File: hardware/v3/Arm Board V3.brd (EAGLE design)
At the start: 165.1 x 76.2 mm, 75 parts, among them CN1 1X4-BIG, IC1 L6206D, IC2 L6206D, IC3 L6206D, IC4 7812TV, IC5 7812TV, IC6 7812TV, IC7 7812DT, IC9 7812DT, Q3 Q_LTC490, U1 MAX3468CPA, U2 XBEE-1B3

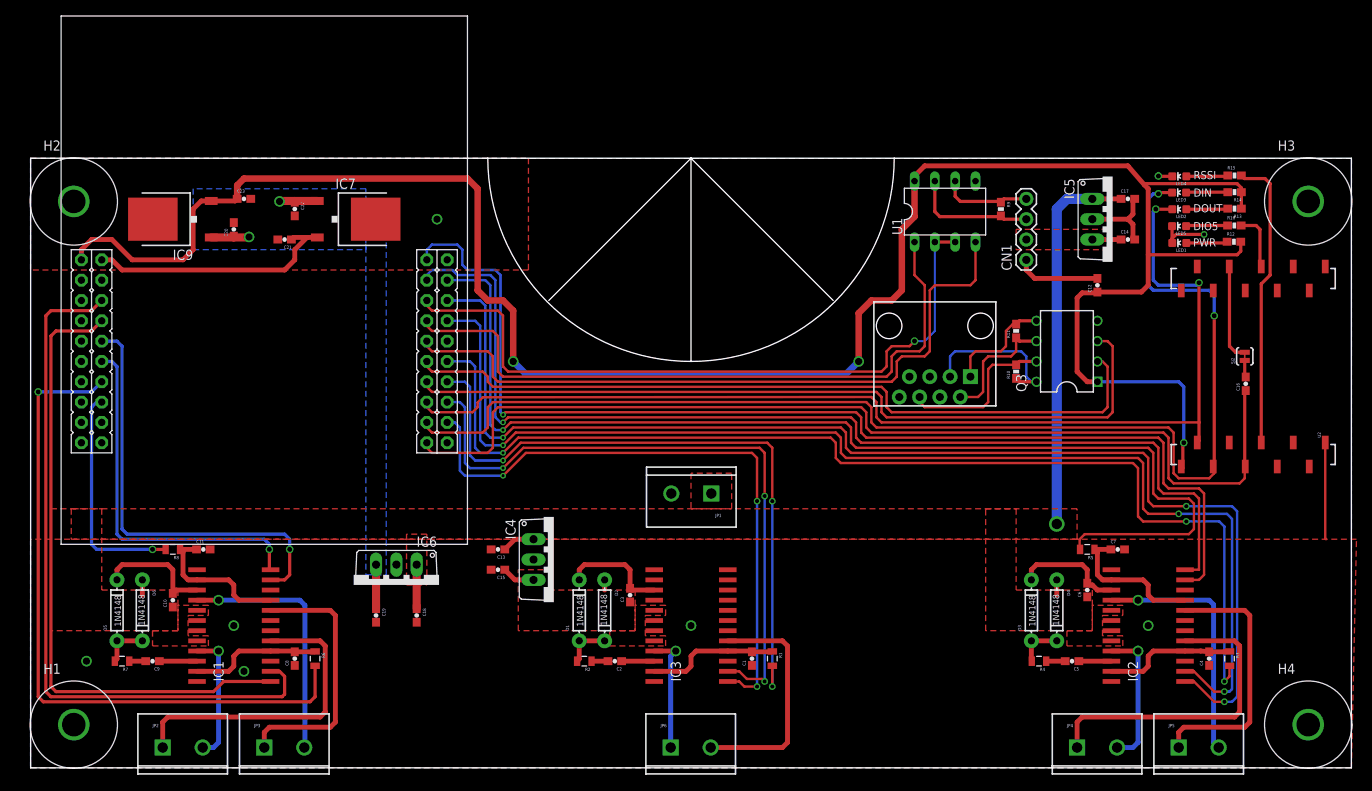
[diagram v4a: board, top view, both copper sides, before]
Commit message: Made some traces bigger
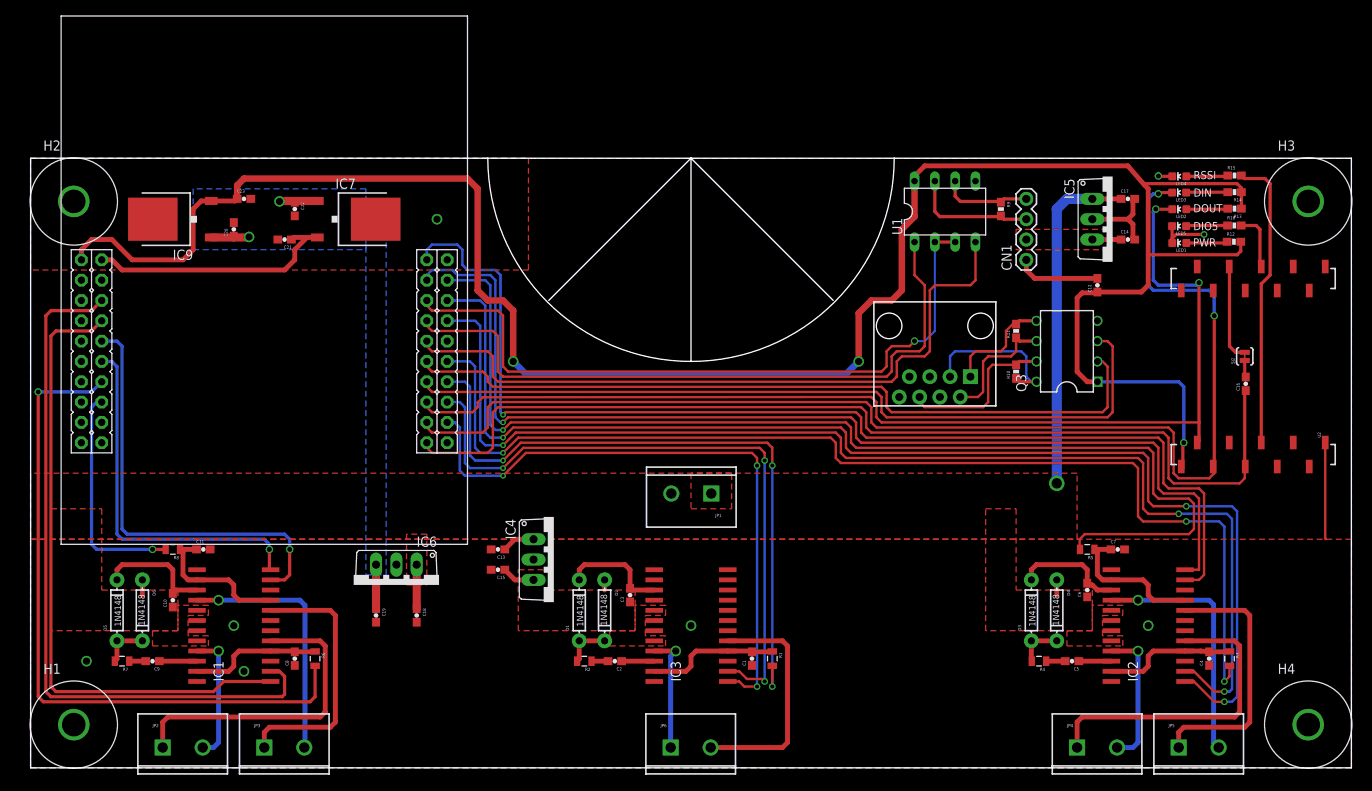
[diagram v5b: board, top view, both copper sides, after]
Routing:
- net VIN: track 61.4 -> 56.3 mm
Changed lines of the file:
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@@
 <vertex x="0" y="0"/>
 <vertex x="165.1" y="0"/>
-<vertex x="165.735" y="28.575"/>
+<vertex x="165.1" y="28.575"/>
 </polygon>
 <contactref element="Q3" pad="4"/>
@@
 </polygon>
 <polygon width="0.4064" layer="1">
-<vertex x="5.08" y="32.385"/>
-<vertex x="5.08" y="28.575"/>
+<vertex x="0" y="36.83"/>
+<vertex x="0" y="28.575"/>
 <vertex x="130.81" y="28.575"/>
-<vertex x="130.81" y="32.385"/>
+<vertex x="130.81" y="36.83"/>
 </polygon>
 <polygon width="0.4064" layer="1" thermals="no">
@@
 <wire x1="132.715" y1="71.12" x2="129.54" y2="71.12" width="1.27" layer="16"/>
 <wire x1="129.54" y1="71.12" x2="128.27" y2="69.85" width="1.27" layer="16"/>
-<wire x1="128.27" y1="69.85" x2="128.27" y2="30.48" width="1.27" layer="16"/>
-<via x="128.27" y="30.48" extent="1-16" drill="1.3" shape="octagon"/>
+<wire x1="128.27" y1="69.85" x2="128.27" y2="35.56" width="1.27" layer="16"/>
+<via x="128.27" y="35.56" extent="1-16" drill="1.3" shape="octagon"/>
 <contactref element="C13" pad="1"/>
 <contactref element="C17" pad="1"/>
@@
 <wire x1="89.2175" y1="10.16" x2="90.805" y2="10.16" width="0.3048" layer="1"/>
 <via x="90.805" y="10.16" extent="1-16" drill="0.5" shape="octagon"/>
-<wire x1="90.805" y1="10.16" x2="90.805" y2="33.3375" width="0.3048" layer="16"/>
-<via x="90.805" y="33.3375" extent="1-16" drill="0.5" shape="octagon"/>
-<wire x1="90.805" y1="33.3375" x2="90.805" y2="38.735" width="0.3048" layer="1"/>
+<wire x1="90.805" y1="10.16" x2="90.805" y2="37.7825" width="0.3048" layer="16"/>
+<via x="90.805" y="37.7825" extent="1-16" drill="0.5" shape="octagon"/>
+<wire x1="90.805" y1="37.7825" x2="90.805" y2="38.735" width="0.3048" layer="1"/>
 <wire x1="90.805" y1="38.735" x2="90.17" y2="39.37" width="0.3048" layer="1"/>
 <wire x1="90.17" y1="39.37" x2="61.9125" y2="39.37" width="0.3048" layer="1"/>
@@
 <contactref element="IC3" pad="2"/>
 <via x="91.7575" y="10.795" extent="1-16" drill="0.5" shape="octagon"/>
-<wire x1="91.7575" y1="10.795" x2="91.7575" y2="33.9725" width="0.3048" layer="16"/>
-<via x="91.7575" y="33.9725" extent="1-16" drill="0.5" shape="octagon"/>
-<wire x1="91.7575" y1="33.9725" x2="91.7575" y2="39.37" width="0.3048" layer="1"/>
+<wire x1="91.7575" y1="10.795" x2="91.7575" y2="38.4175" width="0.3048" layer="16"/>
+<via x="91.7575" y="38.4175" extent="1-16" drill="0.5" shape="octagon"/>
+<wire x1="91.7575" y1="38.4175" x2="91.7575" y2="39.37" width="0.3048" layer="1"/>
 <wire x1="91.7575" y1="39.37" x2="91.1225" y2="40.005" width="0.3048" layer="1"/>
 <wire x1="87.15" y1="12.065" x2="88.5825" y2="12.065" width="0.3048" layer="1"/>
@@
 <wire x1="92.71" y1="12.7525" x2="92.71" y2="10.16" width="0.3048" layer="1"/>
 <via x="92.71" y="10.16" extent="1-16" drill="0.5" shape="octagon"/>
-<wire x1="92.71" y1="10.16" x2="92.71" y2="33.3375" width="0.3048" layer="16"/>
-<via x="92.71" y="33.3375" extent="1-16" drill="0.5" shape="octagon"/>
-<wire x1="92.71" y1="33.3375" x2="92.71" y2="40.005" width="0.3048" layer="1"/>
+<wire x1="92.71" y1="10.16" x2="92.71" y2="37.7825" width="0.3048" layer="16"/>
+<via x="92.71" y="37.7825" extent="1-16" drill="0.5" shape="octagon"/>
+<wire x1="92.71" y1="37.7825" x2="92.71" y2="40.005" width="0.3048" layer="1"/>
 <wire x1="92.71" y1="40.005" x2="92.075" y2="40.64" width="0.3048" layer="1"/>
 <wire x1="92.075" y1="40.64" x2="61.2775" y2="40.64" width="0.3048" layer="1"/>

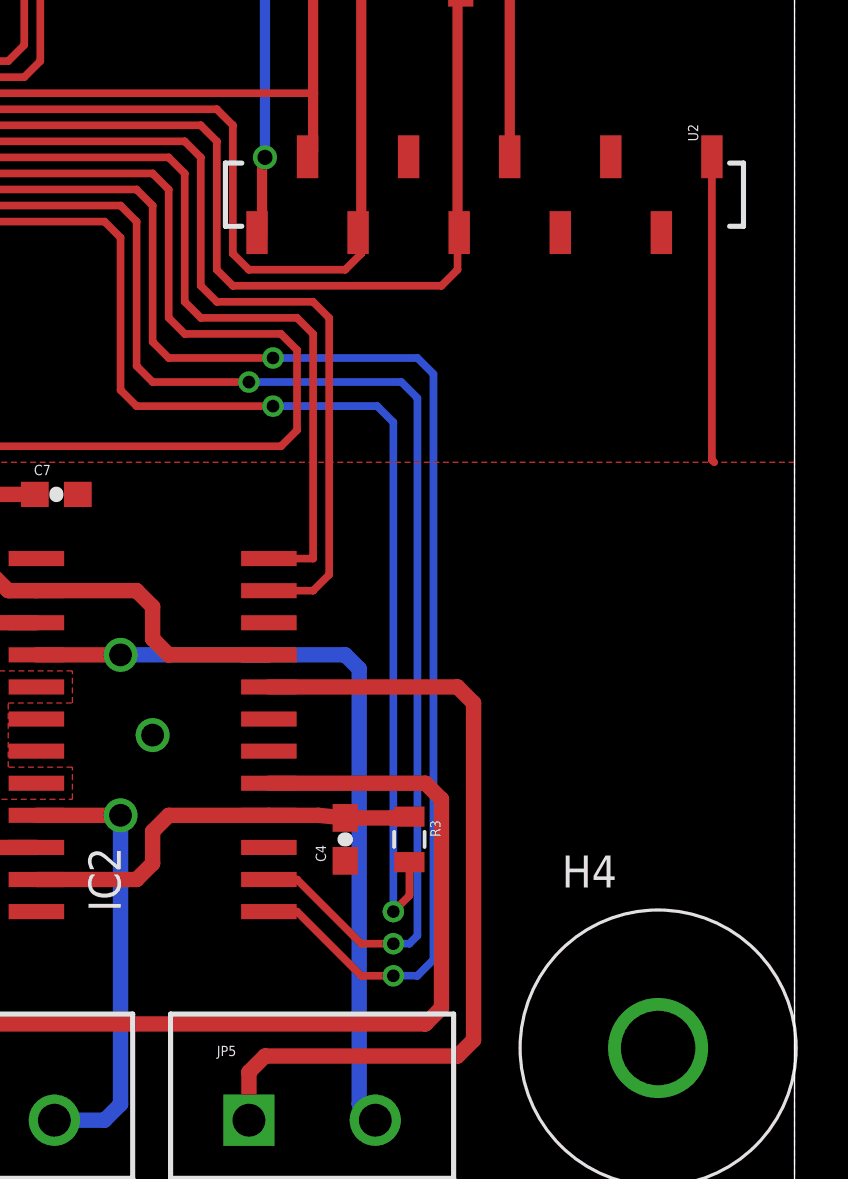
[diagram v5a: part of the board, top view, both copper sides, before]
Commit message: Added RS485 jack next to Xbee
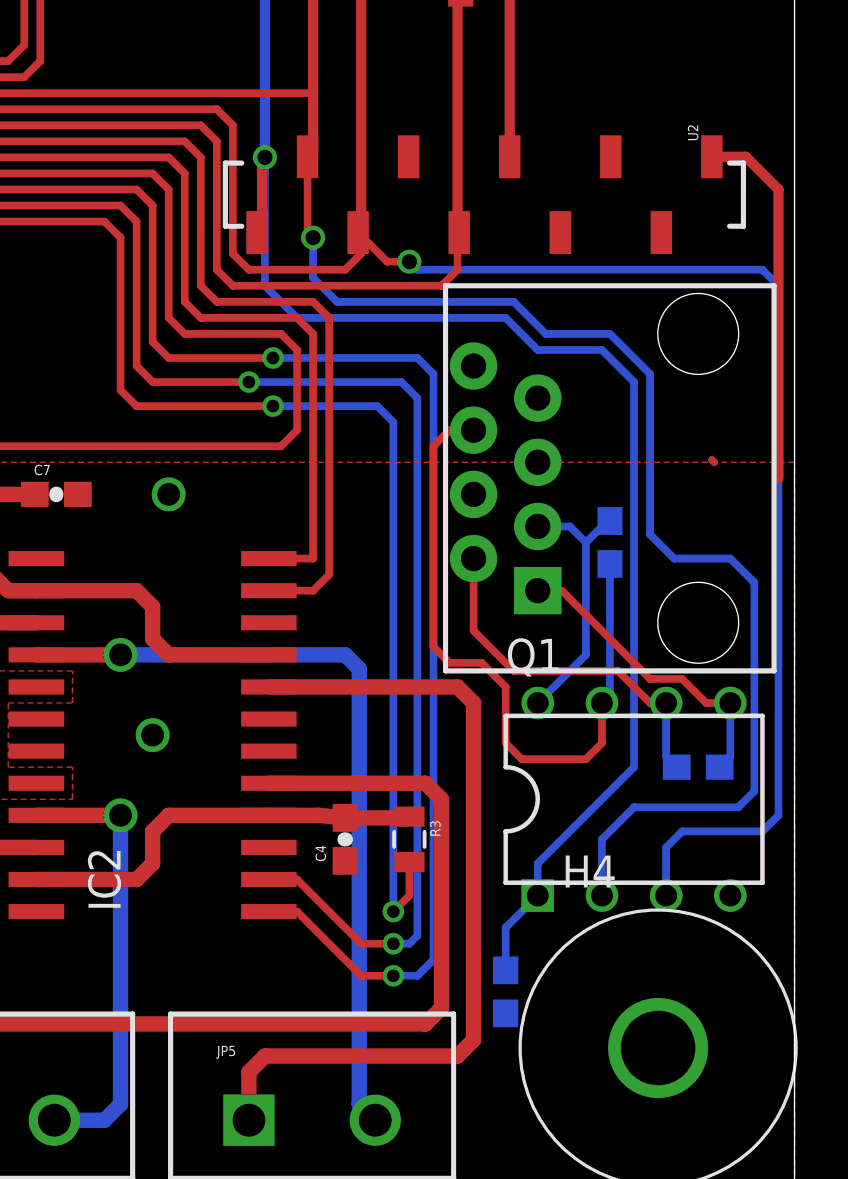
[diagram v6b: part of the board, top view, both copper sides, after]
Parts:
- added C24: .1uF, SparkFun-Capacitors:0603-CAP
- added Q1: Q_LTC490, PCB0M1:DIP8
- added R17, R18: 120 Ohm, SparkFun-Passives:0603-RES
- added U$2: RJ45-8PTH, SparkFun-Connectors:RJ45-8
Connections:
- new net N$12: Q1.5, R18.2, U$2.1
- new net N$14: Q1.6, R18.1, U$2.2
- new net N$20: Q1.7, R17.2, U$2.6
- new net N$21: Q1.8, R17.1, U$2.3
- net +3V3: now also C24.1, Q1.1
- net GND: now also C24.2, Q1.4, U$2.7, U$2.8
- net RXD3: now also Q1.2
- net TXD3: now also Q1.3
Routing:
- net RXD3: track 138.2 -> 186.6 mm, vias 2 -> 3
- net +3V3: track 272.1 -> 318.7 mm
- net TXD3: track 155.9 -> 201.2 mm, vias 2 -> 3
- net N$20: track 0.00 -> 27.1 mm
- net N$14: track 0.00 -> 14.4 mm
- net N$12: track 0.00 -> 12.2 mm
- net N$21: track 0.00 -> 10.6 mm
- net GND: track 41.9 -> 44.5 mm, vias 8 -> 9
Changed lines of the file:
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@@
 </element>
 <element name="IC9" library="linear" package="TO252" value="7812DT" x="17.78" y="68.58" rot="R90"/>
+<element name="U$2" library="SparkFun-Connectors" package="RJ45-8" value="RJ45-8PTH" x="161.29" y="27.94" rot="R90"/>
+<element name="R17" library="SparkFun-Passives" package="0603-RES" value="120 Ohm" x="157.7975" y="25.4" rot="MR270"/>
+<element name="Q1" library="PCB0M1" package="DIP8" value="Q_LTC490" x="158.75" y="15.24"/>
+<element name="R18" library="SparkFun-Passives" package="0603-RES" value="120 Ohm" x="161.29" y="16.51" rot="MR180"/>
+<element name="C24" library="SparkFun-Capacitors" package="0603-CAP" value=".1uF" x="153.67" y="7.62" rot="MR270">
+<attribute name="PROD_ID" value="CAP-08604" x="139.7" y="55.88" size="1.778" layer="28" rot="MR270" display="off"/>
+</element>
 </elements>
 <signals>
@@
 <wire x1="137.795" y1="67.945" x2="137.795" y2="66.255" width="0.6096" layer="1"/>
 <wire x1="137.795" y1="66.255" x2="138.01" y2="66.04" width="0.6096" layer="1"/>
-<wire x1="161.83" y1="40.665" x2="161.83" y2="28.67" width="0.3048" layer="1"/>
 <wire x1="161.83" y1="28.67" x2="161.925" y2="28.575" width="0.3048" layer="1"/>
 <contactref element="C18" pad="2"/>
@@
 <wire x1="125.515" y1="61.175" x2="124.46" y2="62.23" width="0.6096" layer="1"/>
 <wire x1="124.46" y1="62.23" x2="124.46" y2="63.5" width="0.6096" layer="1"/>
+<contactref element="Q1" pad="4"/>
+<contactref element="C24" pad="2"/>
+<contactref element="U$2" pad="8"/>
+<contactref element="U$2" pad="7"/>
+<wire x1="161.83" y1="40.665" x2="163.17" y2="40.665" width="0.4064" layer="1"/>
+<wire x1="163.17" y1="40.665" x2="164.465" y2="39.37" width="0.4064" layer="1"/>
+<wire x1="164.465" y1="39.37" x2="164.465" y2="27.94" width="0.4064" layer="1"/>
+<via x="140.335" y="27.305" extent="1-16" drill="0.9" shape="octagon"/>
 </signal>
 <signal name="A1_1">
@@
 <wire x1="147.955" y1="36.83" x2="147.955" y2="37.54" width="0.3048" layer="1"/>
 <wire x1="147.955" y1="37.54" x2="147.83" y2="37.665" width="0.3048" layer="1"/>
+<contactref element="Q1" pad="3"/>
+<wire x1="160.02" y1="11.43" x2="160.02" y2="13.335" width="0.3048" layer="16"/>
+<wire x1="160.02" y1="13.335" x2="160.655" y2="13.97" width="0.3048" layer="16"/>
+<wire x1="160.655" y1="13.97" x2="163.83" y2="13.97" width="0.3048" layer="16"/>
+<wire x1="163.83" y1="13.97" x2="164.465" y2="14.605" width="0.3048" layer="16"/>
+<wire x1="164.465" y1="14.605" x2="164.465" y2="35.56" width="0.3048" layer="16"/>
+<wire x1="164.465" y1="35.56" x2="163.83" y2="36.195" width="0.3048" layer="16"/>
+<wire x1="163.83" y1="36.195" x2="150.1775" y2="36.195" width="0.3048" layer="16"/>
+<wire x1="150.1775" y1="36.195" x2="149.86" y2="36.5125" width="0.3048" layer="16"/>
+<via x="149.86" y="36.5125" extent="1-16" drill="0.6" shape="square"/>
+<wire x1="149.86" y1="36.5125" x2="148.9825" y2="36.5125" width="0.3048" layer="1"/>
+<wire x1="148.9825" y1="36.5125" x2="147.83" y2="37.665" width="0.3048" layer="1"/>
 </signal>
 <signal name="RXD3">
@@
 <wire x1="140.97" y1="60.325" x2="145.7325" y2="60.325" width="0.4064" layer="16"/>
 <wire x1="145.7325" y1="60.325" x2="146.05" y2="60.6425" width="0.4064" layer="16"/>
+<contactref element="Q1" pad="2"/>
+<wire x1="145.83" y1="40.665" x2="145.83" y2="37.685" width="0.3048" layer="1"/>
+<wire x1="145.83" y1="37.685" x2="146.05" y2="37.465" width="0.3048" layer="1"/>
+<via x="146.05" y="37.465" extent="1-16" drill="0.6" shape="square"/>
+<wire x1="146.05" y1="37.465" x2="146.05" y2="35.8775" width="0.3048" layer="16"/>
+<wire x1="146.05" y1="35.8775" x2="147.0025" y2="34.925" width="0.3048" layer="16"/>
+<wire x1="147.0025" y1="34.925" x2="153.9875" y2="34.925" width="0.3048" layer="16"/>
+<wire x1="153.9875" y1="34.925" x2="155.2575" y2="33.655" width="0.3048" layer="16"/>
+<wire x1="155.2575" y1="33.655" x2="157.7975" y2="33.655" width="0.3048" layer="16"/>
+<wire x1="157.7975" y1="33.655" x2="159.385" y2="32.0675" width="0.3048" layer="16"/>
+<wire x1="159.385" y1="32.0675" x2="159.385" y2="25.7175" width="0.3048" layer="16"/>
+<wire x1="159.385" y1="25.7175" x2="160.3375" y2="24.765" width="0.3048" layer="16"/>
+<wire x1="160.3375" y1="24.765" x2="162.56" y2="24.765" width="0.3048" layer="16"/>
+<wire x1="162.56" y1="24.765" x2="163.5125" y2="23.8125" width="0.3048" layer="16"/>
+<wire x1="163.5125" y1="23.8125" x2="163.5125" y2="15.5575" width="0.3048" layer="16"/>
+<wire x1="163.5125" y1="15.5575" x2="162.8775" y2="14.9225" width="0.3048" layer="16"/>
+<wire x1="162.8775" y1="14.9225" x2="158.75" y2="14.9225" width="0.3048" layer="16"/>
+<wire x1="158.75" y1="14.9225" x2="157.48" y2="13.6525" width="0.3048" layer="16"/>
+<wire x1="157.48" y1="13.6525" x2="157.48" y2="11.43" width="0.3048" layer="16"/>
 </signal>
 <signal name="+3V3">
@@
 <wire x1="133.35" y1="59.475" x2="138.85" y2="59.475" width="0.6096" layer="1"/>
 <wire x1="138.85" y1="59.475" x2="139.7" y2="60.325" width="0.6096" layer="1"/>
+<contactref element="Q1" pad="1"/>
+<contactref element="C24" pad="1"/>
+<wire x1="153.67" y1="8.47" x2="153.67" y2="10.16" width="0.3048" layer="16"/>
+<wire x1="153.67" y1="10.16" x2="154.94" y2="11.43" width="0.3048" layer="16"/>
+<wire x1="154.94" y1="11.43" x2="154.94" y2="12.7" width="0.3048" layer="16"/>
+<wire x1="154.94" y1="12.7" x2="158.75" y2="16.51" width="0.3048" layer="16"/>
+<wire x1="158.75" y1="16.51" x2="158.75" y2="31.75" width="0.3048" layer="16"/>
+<wire x1="158.75" y1="31.75" x2="157.48" y2="33.02" width="0.3048" layer="16"/>
+<wire x1="157.48" y1="33.02" x2="154.94" y2="33.02" width="0.3048" layer="16"/>
+<wire x1="154.94" y1="33.02" x2="153.67" y2="34.29" width="0.3048" layer="16"/>
+<wire x1="153.67" y1="34.29" x2="145.415" y2="34.29" width="0.3048" layer="16"/>
+<wire x1="145.415" y1="34.29" x2="144.145" y2="35.56" width="0.3048" layer="16"/>
+<wire x1="144.145" y1="35.56" x2="144.145" y2="40.64" width="0.3048" layer="16"/>
 </signal>
 <signal name="N$5">
@@
 <wire x1="33.02" y1="70.7" x2="33.02" y2="70.86" width="0.6096" layer="1"/>
 </signal>
+<signal name="N$12">
+<contactref element="Q1" pad="5"/>
+<contactref element="U$2" pad="1"/>
+<contactref element="R18" pad="2"/>
+<wire x1="162.56" y1="19.05" x2="161.6075" y2="19.05" width="0.3048" layer="1"/>
+<wire x1="161.6075" y1="19.05" x2="160.655" y2="20.0025" width="0.3048" layer="1"/>
+<wire x1="160.655" y1="20.0025" x2="159.385" y2="20.0025" width="0.3048" layer="1"/>
+<wire x1="159.385" y1="20.0025" x2="155.8925" y2="23.495" width="0.3048" layer="1"/>
+<wire x1="155.8925" y1="23.495" x2="154.94" y2="23.495" width="0.3048" layer="1"/>
+<wire x1="162.56" y1="19.05" x2="162.56" y2="16.93" width="0.3048" layer="16"/>
+<wire x1="162.56" y1="16.93" x2="162.14" y2="16.51" width="0.3048" layer="16"/>
+</signal>
+<signal name="N$14">
+<contactref element="Q1" pad="6"/>
+<contactref element="U$2" pad="2"/>
+<contactref element="R18" pad="1"/>
+<wire x1="160.02" y1="19.05" x2="159.385" y2="19.05" width="0.3048" layer="1"/>
+<wire x1="159.385" y1="19.05" x2="158.115" y2="20.32" width="0.3048" layer="1"/>
+<wire x1="158.115" y1="20.32" x2="153.9875" y2="20.32" width="0.3048" layer="1"/>
+<wire x1="153.9875" y1="20.32" x2="152.4" y2="21.9075" width="0.3048" layer="1"/>
+<wire x1="152.4" y1="21.9075" x2="152.4" y2="24.765" width="0.3048" layer="1"/>
+<wire x1="160.02" y1="19.05" x2="160.02" y2="16.93" width="0.3048" layer="16"/>
+<wire x1="160.02" y1="16.93" x2="160.44" y2="16.51" width="0.3048" layer="16"/>
+</signal>
+<signal name="N$20">
+<contactref element="Q1" pad="7"/>
+<contactref element="U$2" pad="6"/>
+<contactref element="R17" pad="2"/>
+<wire x1="152.4" y1="29.845" x2="151.4475" y2="29.845" width="0.3048" layer="1"/>
+<wire x1="151.4475" y1="29.845" x2="150.8125" y2="29.21" width="0.3048" layer="1"/>
+<wire x1="150.8125" y1="29.21" x2="150.8125" y2="21.2725" width="0.3048" layer="1"/>
+<wire x1="150.8125" y1="21.2725" x2="151.4475" y2="20.6375" width="0.3048" layer="1"/>
+<wire x1="151.4475" y1="20.6375" x2="152.7175" y2="20.6375" width="0.3048" layer="1"/>
+<wire x1="152.7175" y1="20.6375" x2="153.67" y2="19.685" width="0.3048" layer="1"/>
+<wire x1="153.67" y1="19.685" x2="153.67" y2="17.4625" width="0.3048" layer="1"/>
+<wire x1="153.67" y1="17.4625" x2="154.305" y2="16.8275" width="0.3048" layer="1"/>
+<wire x1="154.305" y1="16.8275" x2="156.845" y2="16.8275" width="0.3048" layer="1"/>
+<wire x1="156.845" y1="16.8275" x2="157.48" y2="17.4625" width="0.3048" layer="1"/>
+<wire x1="157.48" y1="17.4625" x2="157.48" y2="19.05" width="0.3048" layer="1"/>
+<wire x1="157.7975" y1="24.55" x2="157.7975" y2="19.3675" width="0.3048" layer="16"/>
+<wire x1="157.7975" y1="19.3675" x2="157.48" y2="19.05" width="0.3048" layer="16"/>
+</signal>
+<signal name="N$21">
+<contactref element="Q1" pad="8"/>
+<contactref element="U$2" pad="3"/>
+<contactref element="R17" pad="1"/>
+<wire x1="154.94" y1="19.05" x2="156.845" y2="20.955" width="0.3048" layer="16"/>
+<wire x1="156.845" y1="20.955" x2="156.845" y2="25.4" width="0.3048" layer="16"/>
+<wire x1="156.845" y1="25.4" x2="156.21" y2="26.035" width="0.3048" layer="16"/>
+<wire x1="156.21" y1="26.035" x2="154.94" y2="26.035" width="0.3048" layer="16"/>
+<wire x1="157.7975" y1="26.25" x2="157.695" y2="26.25" width="0.3048" layer="16"/>
+<wire x1="157.695" y1="26.25" x2="156.845" y2="25.4" width="0.3048" layer="16"/>
+</signal>
 </signals>
